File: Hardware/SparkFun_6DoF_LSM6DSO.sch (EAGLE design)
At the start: 30 parts, among them J1 QWIIC_RIGHT_ANGLE, J2 QWIIC_RIGHT_ANGLE, U2 LSM6DS0

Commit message: Fixes input/output labels of respective silk, adds better text description to jumpers
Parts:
- removed JP2: JUMPER-SMT_2_NC_TRACE_SILK, SparkFun-Jumpers:JUMPER-SMT_2_NC_TRACE_SILK
- removed U2: LSM6DS0, temp:LSM6DS0
- added LED: JUMPER-SMT_2_NC_TRACE_SILK, SparkFun-Jumpers:JUMPER-SMT_2_NC_TRACE_SILK
- added U1: LSM6DS0, temp:LSM6DS0
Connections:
- net 3.3V: now also U1.VDDIO; no longer U2.VDDIO
- net CS: now also U1.CS; no longer U2.CS
- net GND: now also LED.1, U1.GND@6, U1.GND@7; no longer JP2.1, U2.GND@6, U2.GND@7
- net INT1: now also U1.INT1; no longer U2.INT1
- net INT2: now also U1.INT2; no longer U2.INT2
- net N$3: now also LED.2; no longer JP2.2
- net OCS: now also U1.OCS_AUX; no longer U2.OCS
- net SCL: now also U1.SCL; no longer U2.SCL
- net SCX: now also U1.SCX; no longer U2.SCX
- net SDA: now also U1.SDA; no longer U2.SDA
- net SDO/SA0: now also U1.SDO/SA0; no longer U2.SDO/SA0
- net SDX: now also U1.SDX; no longer U2.SDX
- net VDD: now also U1.VDD; no longer U2.VDD
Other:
- note added: "0x6B (Default) 0x6A Cut trace and leave bottom unconnected if using SPI."
- note added: "Cut trace to disconnect Power LED."
- note added: "Cut trace to remove I2C pull-up resistors."
- note added: "If downstream SPI devices are hosted by the LSM6DSO, release SCx and SDx from ground by cutting traces."
- note added: "Jumpers"
- note removed: "Address can be: 1101011b (0x6B) 1101010b (0x6A)"
- note removed: "Enable pull-up resistors for I2C operation"
- note removed: "If downstream SPI devices are hosted by the LSM6DS3, release SCx and SDx from ground by opening SJ3 and SJ4."
- moved on the sheet: ADDR, C3, C4, D1, J1, J2, JP1, JP3, L1, R3, R4

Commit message: Adds VDD and VDDIO voltage range to schematic
* Moves some traces and vias that were too close to the standoffs
* Adds SparkFun flame and name of product to topside
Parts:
- LOGO1: value QWIIC_LOGO_3MM -> QWIIC_LOGO_4MM; device SparkFun-Aesthetics:QWIIC_LOGO_3MM -> SparkFun-Aesthetics:QWIIC_LOGO_4MM
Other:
- note added: "Connectors"
- note added: "VDD Range: 1.71V - 3.6V VDDIO Range: 1.62V - 3.6V"
- note removed: "VDD Range: VDDIO Range:"
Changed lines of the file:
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@@
 <part name="FD1" library="SparkFun-Aesthetics" deviceset="FIDUCIAL" device="UFIDUCIAL"/>
 <part name="FD2" library="SparkFun-Aesthetics" deviceset="FIDUCIAL" device="UFIDUCIAL"/>
-<part name="LOGO1" library="SparkFun-Aesthetics" deviceset="QWIIC_LOGO" device="_3MM"/>
+<part name="LOGO1" library="SparkFun-Aesthetics" deviceset="QWIIC_LOGO" device="_4MM" value="QWIIC_LOGO_4MM"/>
 <part name="SUPPLY1" library="SparkFun-PowerSymbols" deviceset="3.3V" device=""/>
 <part name="GND3" library="SparkFun-PowerSymbols" deviceset="GND" device=""/>
@@
 <sheet>
 <plain>
-<text x="26.162" y="175.26" size="2.54" layer="94" font="vector">Accelerometer - LSM6DS0</text>
+<text x="56.642" y="177.8" size="2.54" layer="94" font="vector" align="center">Accelerometer - LSM6DS0</text>
 <text x="245.872" y="121.666" size="1.778" layer="97" font="vector" rot="R180" align="top-left">If downstream SPI devices are
 hosted by the LSM6DSO, release
@@
 <wire x1="114.3" y1="86.36" x2="248.92" y2="86.36" width="0.2032" layer="97" style="longdash"/>
 <wire x1="114.3" y1="185.42" x2="114.3" y2="86.36" width="0.2032" layer="97" style="longdash"/>
-<text x="50.8" y="149.86" size="1.27" layer="97" font="vector">VDD Range:
-VDDIO Range: </text>
+<text x="45.466" y="150.114" size="1.27" layer="97" font="vector">VDD Range: 1.71V - 3.6V
+VDDIO Range: 1.62V - 3.6V</text>
 <text x="238.76" y="7.62" size="2.54" layer="94" font="vector">v10</text>
 <text x="215.646" y="152.146" size="1.778" layer="97" font="vector">0x6B (Default)
@@
 bottom unconnected
 if using SPI.</text>
-<text x="165.1" y="177.8" size="2.54" layer="94" font="vector">Jumpers</text>
+<text x="177.8" y="180.34" size="2.54" layer="94" font="vector" align="center">Jumpers</text>
 <text x="129.54" y="134.62" size="1.778" layer="97" font="vector">Cut trace to
 disconnect Power
 LED.</text>
+<text x="116.84" y="78.74" size="2.54" layer="94" font="vector" align="center">Connectors</text>
 </plain>
 <instances>

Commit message: Updates LSM6D0 with axes, fixes measures, removes references to "slave/master" terminology
* Removes inner standoffs
* Centers IC
* Adds 100k pullup to SDO/SA0 net
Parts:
- added R5: 100k, SparkFun-Resistors:100KOHM-0603-1/10W-1%
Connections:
- removed net CS: JP1.1, R3.1, U1.CS
- new net !CS!: JP1.1, R3.1, U1.!CS!
- new net N$1: ADDR.3, R5.1
- net 3.3V: now also R5.2; no longer ADDR.3
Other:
- note added: "SERIAL MODES MODE1: Perhipheral-only mode I2C or SPI MODE2: Sensor Hub mode I2C or SPI with controller I2C port MODE3: AUX SPI mode I2C and SPI access (Multi-read)"
- note removed: "SERIAL MODES MODE1: Slave-only mode I2C or SPI MODE2: Sensor Hub mode I2C or SPI with master I2C port MODE3: AUX SPI mode I2C and SPI access (Multi-read)"
- moved on the sheet: ADDR
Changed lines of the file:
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@@
 <part name="STANDOFF2" library="SparkFun-Hardware" deviceset="STAND-OFF" device="TIGHT"/>
 <part name="STANDOFF3" library="SparkFun-Hardware" deviceset="STAND-OFF" device="TIGHT"/>
-<part name="STANDOFF4" library="SparkFun-Hardware" deviceset="STAND-OFF" device="TIGHT"/>
 <part name="R1" library="SparkFun-Resistors" deviceset="4.7KOHM" device="-0603-1/10W-1%" value="4.7k"/>
 <part name="R2" library="SparkFun-Resistors" deviceset="4.7KOHM" device="-0603-1/10W-1%" value="4.7k"/>
@@
 <part name="GND7" library="SparkFun-PowerSymbols" deviceset="GND" device=""/>
 <part name="U1" library="temp" deviceset="LSM6DS0" device="" value="LSM6DS0"/>
+<part name="STANDOFF4" library="SparkFun-Hardware" deviceset="STAND-OFF" device="TIGHT"/>
+<part name="R5" library="SparkFun-Resistors" deviceset="100KOHM" device="-0603-1/10W-1%" value="100k"/>
 </parts>
 <sheets>
@@
 pull-up resistors.</text>
 <text x="38.1" y="109.22" size="1.778" layer="97" font="vector" align="top-left">SERIAL MODES
-MODE1:  Slave-only mode
+MODE1:  Perhipheral-only mode
    I2C or SPI
 MODE2:  Sensor Hub mode
-   I2C or SPI with master I2C port
+   I2C or SPI with controller I2C port
 MODE3:  AUX SPI mode
    I2C and SPI access (Multi-read)   </text>
@@
 VDDIO Range: 1.62V - 3.6V</text>
 <text x="238.76" y="7.62" size="2.54" layer="94" font="vector">v10</text>
-<text x="215.646" y="152.146" size="1.778" layer="97" font="vector">0x6B (Default)
+<text x="215.646" y="141.986" size="1.778" layer="97" font="vector">0x6B (Default)
 0x6A
 Cut trace and leave
@@
 <attribute name="VALUE" x="16.764" y="132.461" size="1.778" layer="96" font="vector"/>
 </instance>
-<instance part="ADDR" gate="G$1" x="213.36" y="162.56" smashed="yes" rot="MR180">
-<attribute name="NAME" x="215.646" y="167.513" size="1.778" layer="95" font="vector" rot="MR180"/>
-</instance>
-<instance part="GND6" gate="1" x="213.36" y="149.86" smashed="yes" rot="MR0">
-<attribute name="VALUE" x="215.9" y="147.32" size="1.778" layer="96" font="vector" rot="MR0"/>
+<instance part="ADDR" gate="G$1" x="213.36" y="152.4" smashed="yes" rot="MR180">
+<attribute name="NAME" x="215.646" y="157.353" size="1.778" layer="95" font="vector" rot="MR180"/>
+</instance>
+<instance part="GND6" gate="1" x="213.36" y="139.7" smashed="yes" rot="MR0">
+<attribute name="VALUE" x="215.9" y="137.16" size="1.778" layer="96" font="vector" rot="MR0"/>
 </instance>
 <instance part="SUPPLY10" gate="G$1" x="213.36" y="172.72" smashed="yes" rot="MR0">
@@
 <instance part="STANDOFF2" gate="G$1" x="238.76" y="30.48" smashed="yes"/>
 <instance part="STANDOFF3" gate="G$1" x="241.3" y="30.48" smashed="yes"/>
-<instance part="STANDOFF4" gate="G$1" x="243.84" y="30.48" smashed="yes"/>
 <instance part="R1" gate="G$1" x="132.08" y="101.6" smashed="yes" rot="R90">
 <attribute name="NAME" x="130.5814" y="97.79" size="1.778" layer="95" font="vector" rot="R90"/>
@@
 <attribute name="VALUE" x="29.464" y="54.356" size="1.778" layer="96" font="vector"/>
 </instance>
-<instance part="GND11" gate="1" x="30.48" y="25.4" smashed="yes">
-<attribute name="VALUE" x="27.94" y="22.86" size="1.778" layer="96" font="vector"/>
+<instance part="GND11" gate="1" x="30.48" y="30.48" smashed="yes">
+<attribute name="VALUE" x="27.94" y="27.94" size="1.778" layer="96" font="vector"/>
 </instance>
 <instance part="R3" gate="G$1" x="76.2" y="149.86" smashed="yes" rot="R90">
@@
 <instance part="FD2" gate="G$1" x="243.84" y="25.4" smashed="yes"/>
 <instance part="LOGO1" gate="G$1" x="190.5" y="50.8" smashed="yes"/>
-<instance part="SUPPLY1" gate="G$1" x="88.9" y="60.96" smashed="yes">
-<attribute name="VALUE" x="87.884" y="64.516" size="1.778" layer="96" font="vector"/>
+<instance part="SUPPLY1" gate="G$1" x="88.9" y="58.42" smashed="yes">
+<attribute name="VALUE" x="87.884" y="61.976" size="1.778" layer="96" font="vector"/>
 </instance>
 <instance part="GND3" gate="1" x="86.36" y="25.4" smashed="yes">
@@
 <attribute name="NAME" x="50.8" y="145.288" size="1.778" layer="95" font="vector"/>
 <attribute name="VALUE" x="50.8" y="119.38" size="1.778" layer="96" font="vector"/>
+</instance>
+<instance part="STANDOFF4" gate="G$1" x="243.84" y="30.48" smashed="yes"/>
+<instance part="R5" gate="G$1" x="213.36" y="165.1" smashed="yes" rot="R90">
+<attribute name="NAME" x="211.836" y="165.1" size="1.778" layer="95" font="vector" rot="R90" align="bottom-center"/>
+<attribute name="VALUE" x="214.884" y="165.1" size="1.778" layer="96" font="vector" rot="R90" align="top-center"/>
 </instance>
 </instances>
@@
 <wire x1="27.94" y1="35.56" x2="30.48" y2="35.56" width="0.1524" layer="91"/>
 <pinref part="GND11" gate="1" pin="GND"/>
-<wire x1="30.48" y1="35.56" x2="30.48" y2="27.94" width="0.1524" layer="91"/>
+<wire x1="30.48" y1="35.56" x2="30.48" y2="33.02" width="0.1524" layer="91"/>
 <pinref part="JP1" gate="G$1" pin="6"/>
 </segment>
@@
 <pinref part="ADDR" gate="G$1" pin="1"/>
 <pinref part="GND6" gate="1" pin="GND"/>
-<wire x1="213.36" y1="152.4" x2="213.36" y2="157.48" width="0.1524" layer="91"/>
+<wire x1="213.36" y1="142.24" x2="213.36" y2="147.32" width="0.1524" layer="91"/>
 </segment>
 <segment>
@@
 </segment>
 </net>
-<net name="CS" class="0">
+<net name="!CS!" class="0">
 <segment>
 <wire x1="73.66" y1="134.62" x2="76.2" y2="134.62" width="0.1524" layer="91"/>
@@
 <wire x1="78.74" y1="134.62" x2="76.2" y2="134.62" width="0.1524" layer="91"/>
 <junction x="76.2" y="134.62"/>
-<pinref part="U1" gate="G$1" pin="CS"/>
+<pinref part="U1" gate="G$1" pin="!CS!"/>
 </segment>
 <segment>
@@
 <segment>
 <pinref part="ADDR" gate="G$1" pin="2"/>
-<wire x1="208.28" y1="162.56" x2="205.74" y2="162.56" width="0.1524" layer="91"/>
-<label x="205.74" y="162.56" size="1.27" layer="95" font="vector" rot="R180" xref="yes"/>
+<wire x1="208.28" y1="152.4" x2="205.74" y2="152.4" width="0.1524" layer="91"/>
+<label x="205.74" y="152.4" size="1.27" layer="95" font="vector" rot="R180" xref="yes"/>
 </segment>
 </net>
@@
 </net>
 <net name="3.3V" class="0">
-<segment>
-<pinref part="ADDR" gate="G$1" pin="3"/>
-<pinref part="SUPPLY10" gate="G$1" pin="3.3V"/>
-<wire x1="213.36" y1="172.72" x2="213.36" y2="167.64" width="0.1524" layer="91"/>
-</segment>
 <segment>
 <pinref part="SUPPLY4" gate="G$1" pin="3.3V"/>
@@
 <pinref part="SUPPLY1" gate="G$1" pin="3.3V"/>
 <pinref part="J2" gate="G$1" pin="2"/>
-<wire x1="88.9" y1="50.8" x2="88.9" y2="60.96" width="0.1524" layer="91"/>
+<wire x1="88.9" y1="50.8" x2="88.9" y2="58.42" width="0.1524" layer="91"/>
 <wire x1="83.82" y1="50.8" x2="88.9" y2="50.8" width="0.1524" layer="91"/>
 <junction x="88.9" y="50.8"/>
@@
 <pinref part="SUPPLY3" gate="G$1" pin="3.3V"/>
 <wire x1="127" y1="170.18" x2="127" y2="172.72" width="0.1524" layer="91"/>
+</segment>
+<segment>
+<pinref part="SUPPLY10" gate="G$1" pin="3.3V"/>
+<pinref part="R5" gate="G$1" pin="2"/>
+<wire x1="213.36" y1="172.72" x2="213.36" y2="170.18" width="0.1524" layer="91"/>
 </segment>
 </net>
@@
 </segment>
 </net>
+<net name="N$1" class="0">
+<segment>
+<pinref part="ADDR" gate="G$1" pin="3"/>
+<pinref part="R5" gate="G$1" pin="1"/>
+<wire x1="213.36" y1="160.02" x2="213.36" y2="157.48" width="0.1524" layer="91"/>
+</segment>
+</net>

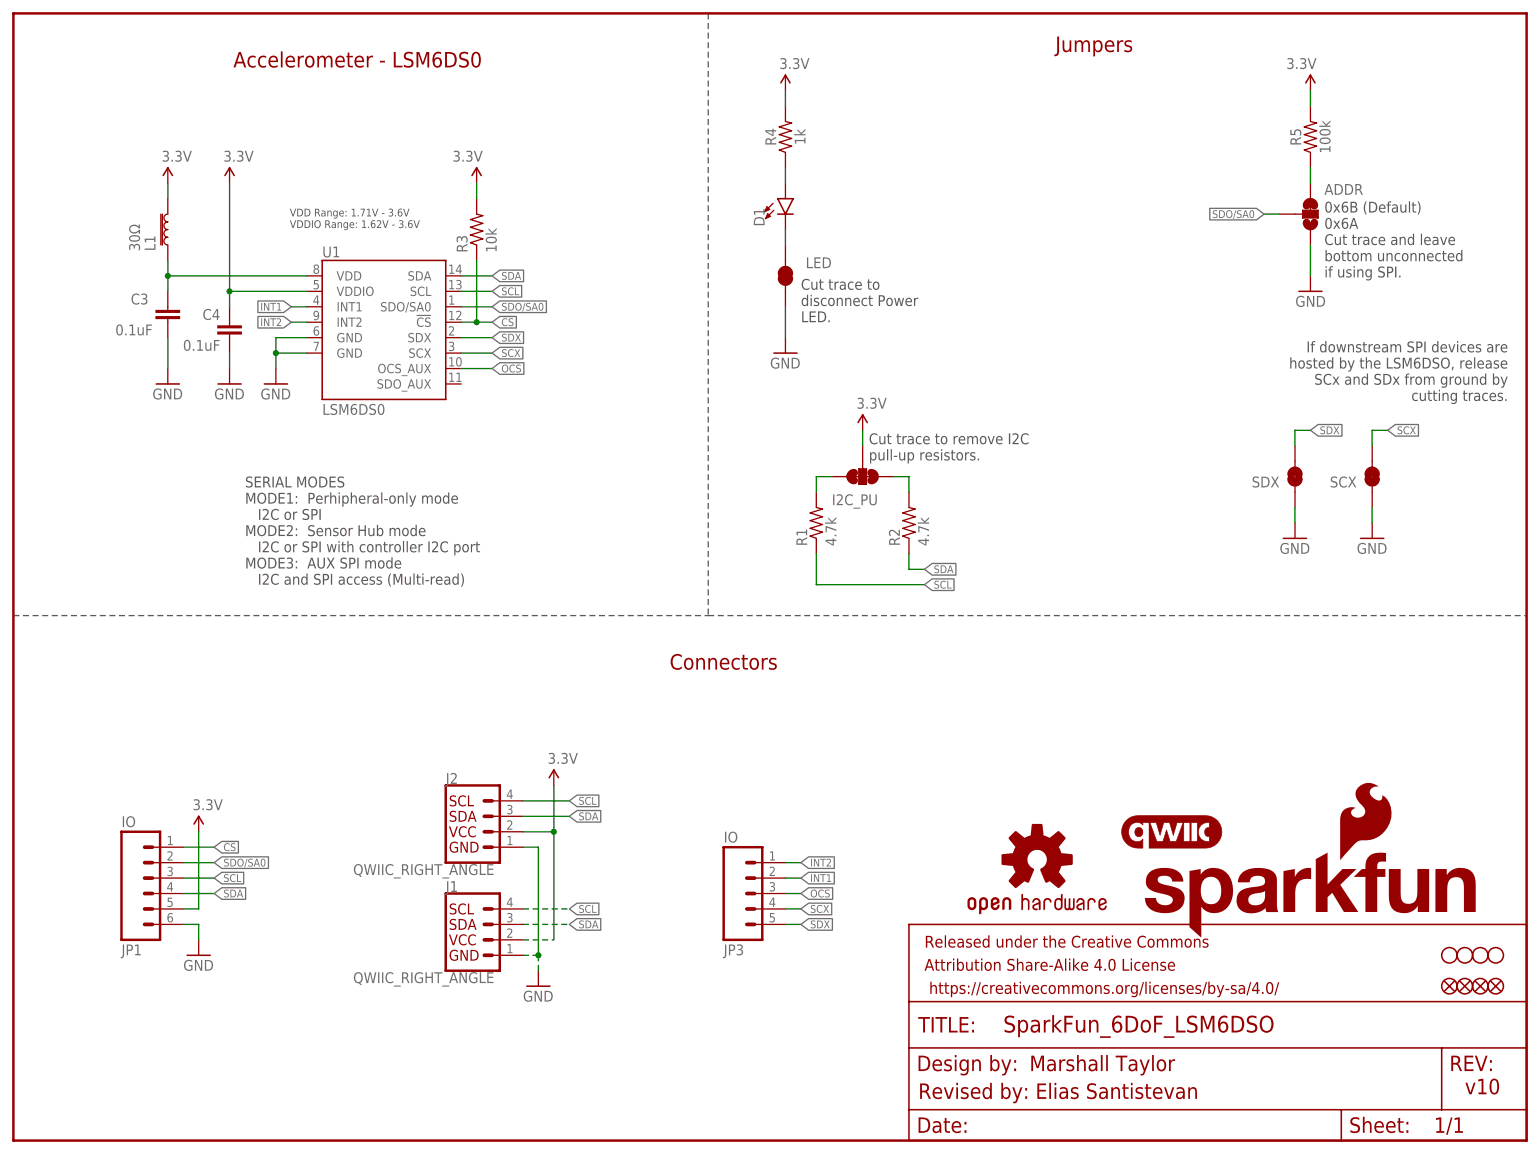
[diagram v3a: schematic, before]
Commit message: Updates IC with production ID, adjusts connector section
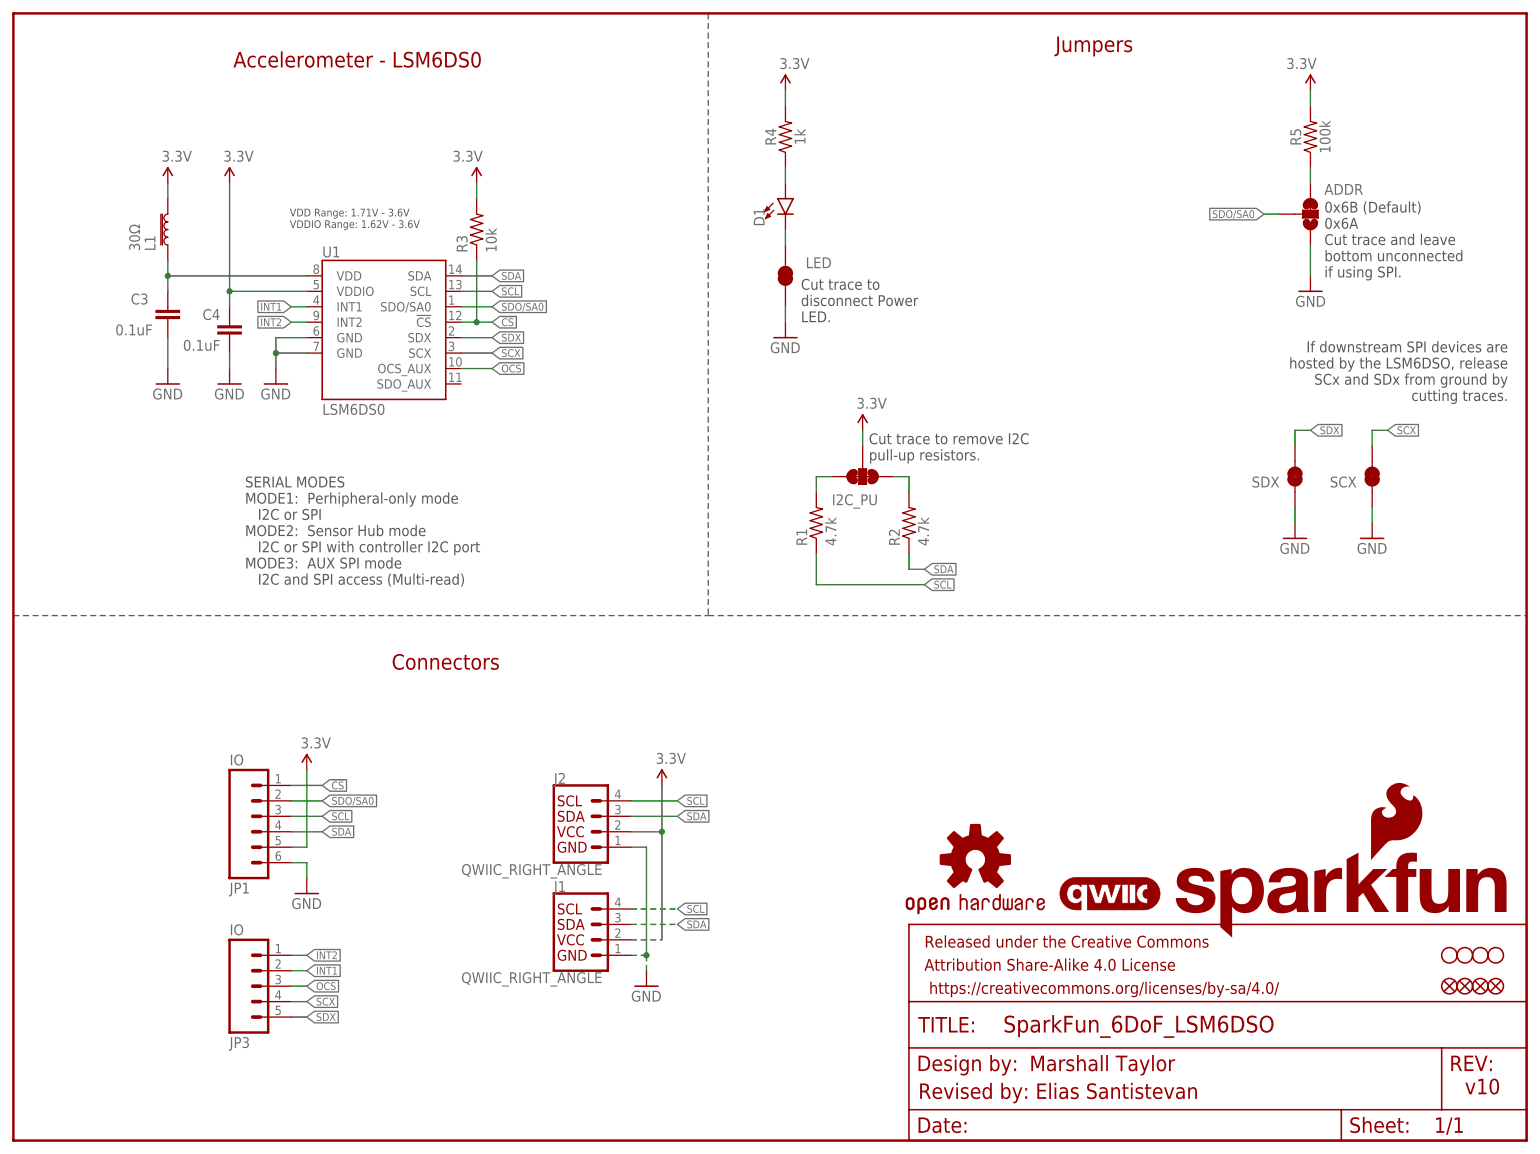
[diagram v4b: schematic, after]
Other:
- moved on the sheet: J1, J2, JP1, JP3
